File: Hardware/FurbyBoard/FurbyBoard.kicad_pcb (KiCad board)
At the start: 4 copper layers, 68.8 x 74.6 mm, 155 parts, among them J1 USB-C 16P, J11 J_EXP: header de expansión si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, J2 BAT+, J3 BAT-, J5 Micro I2S (3V3, GND, SCK, WS,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, J6 FPC 24P 0.5, J7 Frente: IR (emisor ×2, recept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, J8 Inclinación ×3, lengua ×2, al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, J9 Leva ×2, encoder ×4, barriga 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, Q1 SI7615ADN, Q2 AO3400A, Q3 AO3400A, SW1 RESET, SW2 BOOT, U1 USBLC6-2SC6, U10 TCA9535PWR, U11 SN74LVC1G17DBVR, U2 BQ24073RGTR, U3 TPS63802DLAR, U4 ESP32-S3-WROOM-1-N16R8, U5 TPS61089RNRR, U6 DRV8231ADSGR, U7 MAX98357AETE+T, U8 ME6211C28M5G-N, U9 ME6211C12M5G-N

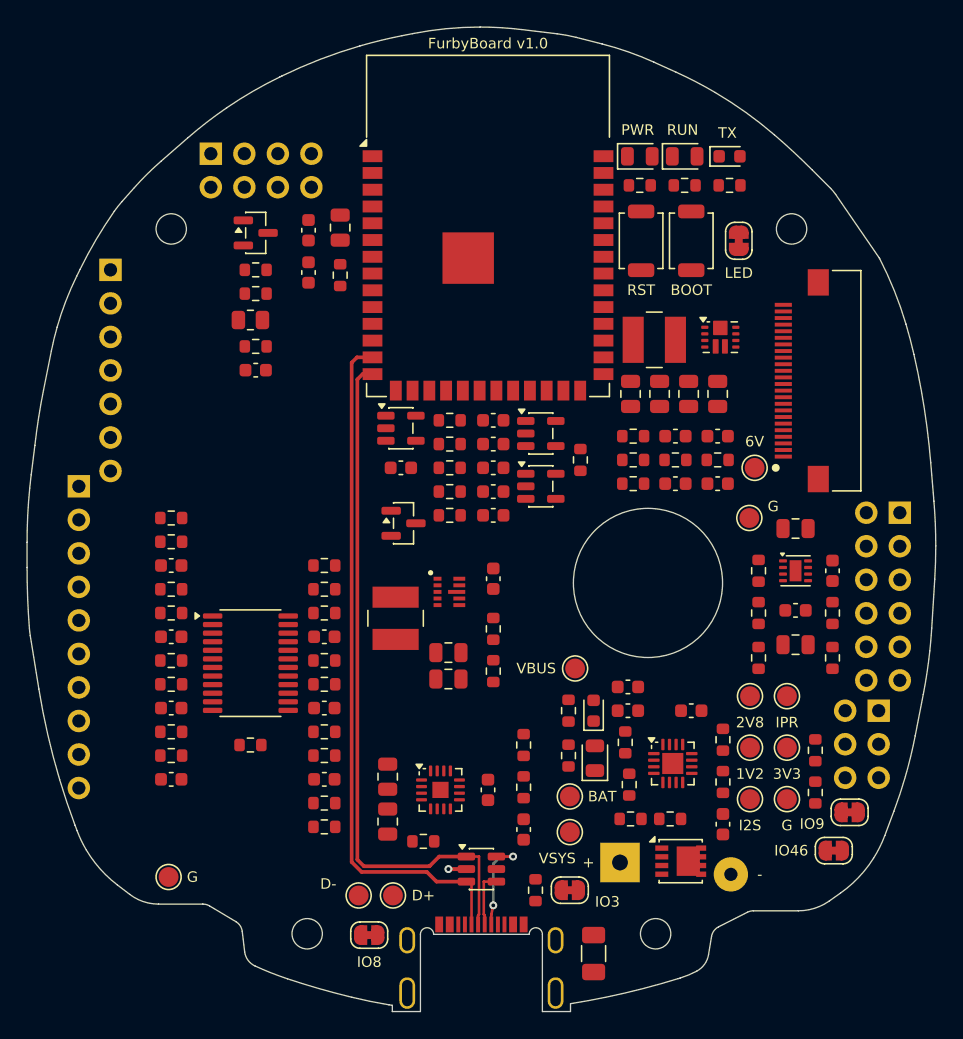
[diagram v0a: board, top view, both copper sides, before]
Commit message: Refactor: elevador de 6 V junto al DRV y al cargador, pasillo libre para la cámara
El bus DVP iba del módulo al FPC cruzando el bloque del TPS61089. El
elevador (U5, L2, C12-C19, R20-R24) pasa a la zona de abajo a la derecha,
entre el cargador (VSYS) y el puente H (V6), con el lazo de entrada y el de
salida cortos. El cargador se reordena con cada pasivo junto a su pin; los
LED de carga, junto al borde de la batería; JP1-JP3 al lóbulo izquierdo y al
del USB-C; R31/R32 junto a J5. comprobar_colocacion.py OK.

Co-Authored-By: Claude Opus 5.5 (1M context) <noreply@anthropic.com>
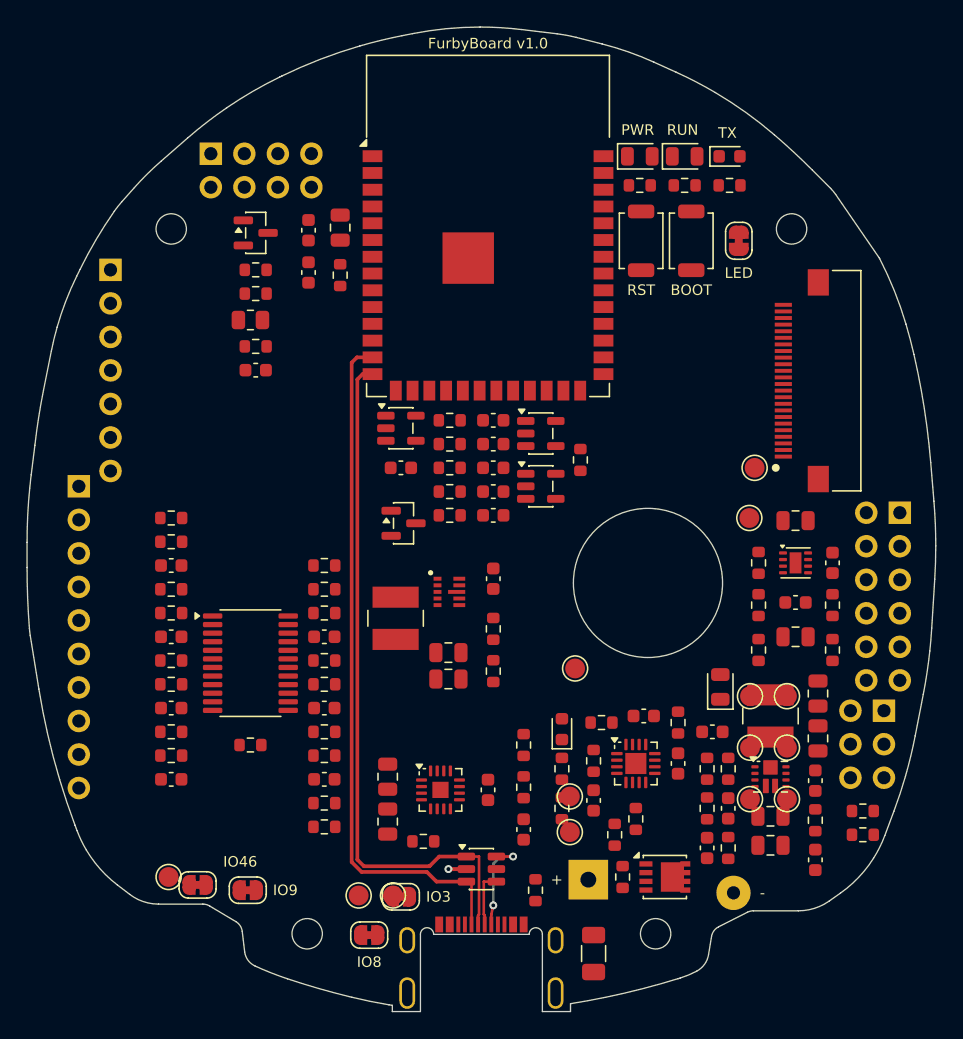
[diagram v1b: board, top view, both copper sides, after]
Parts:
- moved JP2 48.3 mm to (125.0, 78.2)
- moved JP1 46.0 mm to (128.8, 78.6)
- moved C19 34.4 mm to (168.4, 75.2), turned to 0 degrees
- moved U5 33.5 mm to (168.4, 70.0)
- moved C18 32.6 mm to (168.4, 73.0), turned to 0 degrees
- moved R21 30.3 mm to (165.2, 75.4), turned to 90 degrees
- moved L2 29.8 mm to (168.4, 65.4), turned to -90 degrees
- moved C15 29.4 mm to (171.8, 76.3), turned to 90 degrees
- moved C17 28.7 mm to (172.0, 67.1)
- moved C12 28.5 mm to (165.2, 72.4), turned to 90 degrees
- moved R23 28.3 mm to (171.8, 73.3), turned to 90 degrees
- moved C14 27.7 mm to (163.6, 75.4), turned to 90 degrees
- moved C13 27.1 mm to (171.8, 70.3), turned to 90 degrees
- moved C16 26.8 mm to (172.0, 63.7)
- moved R20 26.2 mm to (165.2, 69.4), turned to 90 degrees
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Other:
- board text removed: "1V2"
- board text removed: "2V8"
- board text removed: "6V"
- board text removed: "BAT"
- board text removed: "D+"
- board text removed: "D-"
- board text removed: "I2S"
- board text removed: "IPR"
- board text removed: "VBUS"

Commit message: Refactor: colocación final antes de rutar, con los TP junto a su fuente
- Amplificador (U7) junto a los pines del I2S del módulo y a los pads del
  altavoz (J8); deja libre la zona de abajo a la izquierda.
- Columnas de pasivos del expansor separadas de U10 para dejar pasillo de
  vías de GND.
- TP colocados y fijados antes de rutar: pad de 1,5 mm en la cara inferior
  sobre una vía de su red, junto al pin de su fuente; TP9 en el pin de
  I2S_DOUT del módulo. Lejos del logo y de los tornillos.
- aplicar.py: --fijar bloquea lo aplicado; rellenos exteriores solo con
  --rellenos.
- render/colocacion-arriba.png y colocacion-abajo.png.

DRC 0 infracciones, paridad OK; sin rutar.

Co-Authored-By: Claude Opus 5.5 (1M context) <noreply@anthropic.com>
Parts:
- TP1, TP10, TP11, TP12, TP13, TP14, TP2, TP3, TP4, TP5, TP6, TP7, TP8, TP9: moved to B.Cu
- moved TP9 50.6 mm to (137.0, 30.8), turned to 180 degrees
- moved C26 33.4 mm to (126.6, 44.5)
- moved U7 29.7 mm to (130.0, 44.5)
- moved C25 27.3 mm to (133.4, 46.8)
- moved C24 27.3 mm to (133.4, 43.4)
- moved TP6 27.0 mm to (144.7, 57.6), turned to 180 degrees
- moved TP7 25.2 mm to (168.7, 71.7), turned to 180 degrees
- moved TP10 25.1 mm to (151.9, 43.8), turned to 180 degrees
- moved TP11 25.0 mm to (151.9, 47.8), turned to 180 degrees
- moved TP1 21.3 mm to (155.7, 83.0), turned to 180 degrees
- moved TP13 20.6 mm to (166.0, 71.0), turned to 180 degrees
- moved TP12 20.4 mm to (143.0, 80.2), turned to 180 degrees
- moved TP14 19.4 mm to (170.9, 52.4), turned to 180 degrees
- moved TP8 12.0 mm to (168.0, 52.0), turned to 180 degrees
- moved TP5 8.86 mm to (160.5, 69.2), turned to 180 degrees
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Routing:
- net GND: track 1.36 -> 5.17 mm, vias 1 -> 4
- net IPROPI: track 0.00 -> 1.49 mm, vias 0 -> 1
- net I2S_DOUT: track 0.00 -> 0.89 mm, vias 0 -> 1
- net V6: track 0.00 -> 0.50 mm, vias 0 -> 1
- net VSYS: track 0.00 -> 0.45 mm, vias 0 -> 1
- net USB_DP: track 60.2 -> 60.7 mm, vias 2 -> 3
- net VBUS: track 0.00 -> 0.45 mm, vias 0 -> 1
- net CAM_DVDD: track 0.00 -> 0.45 mm, vias 0 -> 1
- net CAM_2V8: track 0.00 -> 0.45 mm, vias 0 -> 1
- net BAT: track 0.00 -> 0.45 mm, vias 0 -> 1
- net USB_DN: track 56.4 -> 56.8 mm, vias 0 -> 1
- net 3V3: track 0.00 -> 0.45 mm, vias 0 -> 1
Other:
- board text added: "1V2"
- board text added: "2V8"
- board text added: "6V"
- board text added: "BAT"
- board text added: "D+"
- board text added: "D-"
- board text added: "I2S"
- board text added: "VBUS"

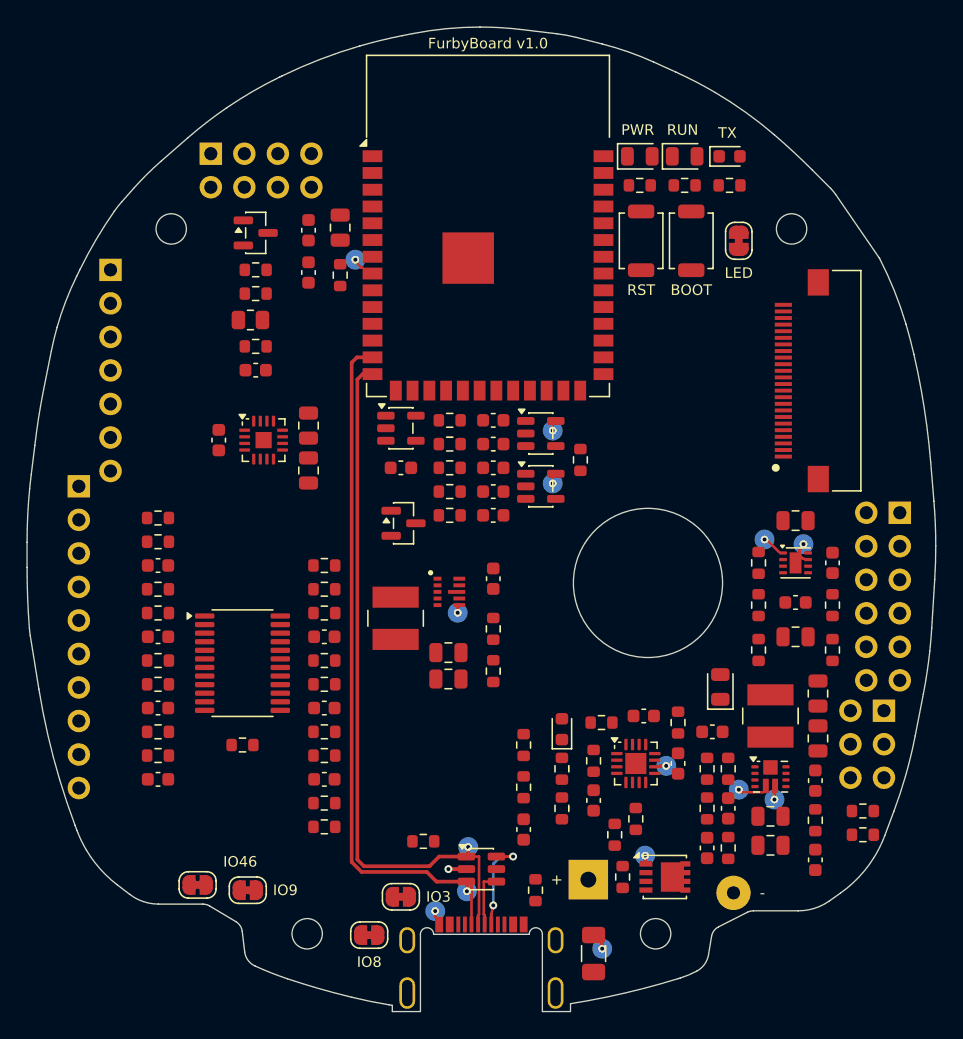
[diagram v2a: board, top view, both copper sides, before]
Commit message: Feature: lo crítico pre-rutado y fijado antes del autorrutado
- preparar.sh: colocación, TP, vías térmicas, pre-rutado y DSN en un paso.
- Pre-rutado con el rutador por rejilla (con su post-proceso) y fijado:
  lazos del TPS61089, del TPS63802 y del puente H, carga, batería, VSYS,
  V6, motor, altavoz, LED IR, 3V3 y bajadas de GND al plano (prerrutado.json,
  con 0,8 mm en los nodos de conmutación y 0,5-0,6 en potencia). C18/C19 giradas
  para que VOUT y GND del TPS61089 caigan sobre su condensador; compensación
  junto a su pin.
- vias_termicas.py: vías bajo los pads expuestos de U2, U7, U6 y U4.
- Amplificador fuera de la zona del logo (no admite vías).
- El DSN sale sin el relleno de VSYS de In2 (si no, tapa la capa).

DRC 0 infracciones, paridad OK; quedan 144 pads por unir.

Co-Authored-By: Claude Opus 5.5 (1M context) <noreply@anthropic.com>
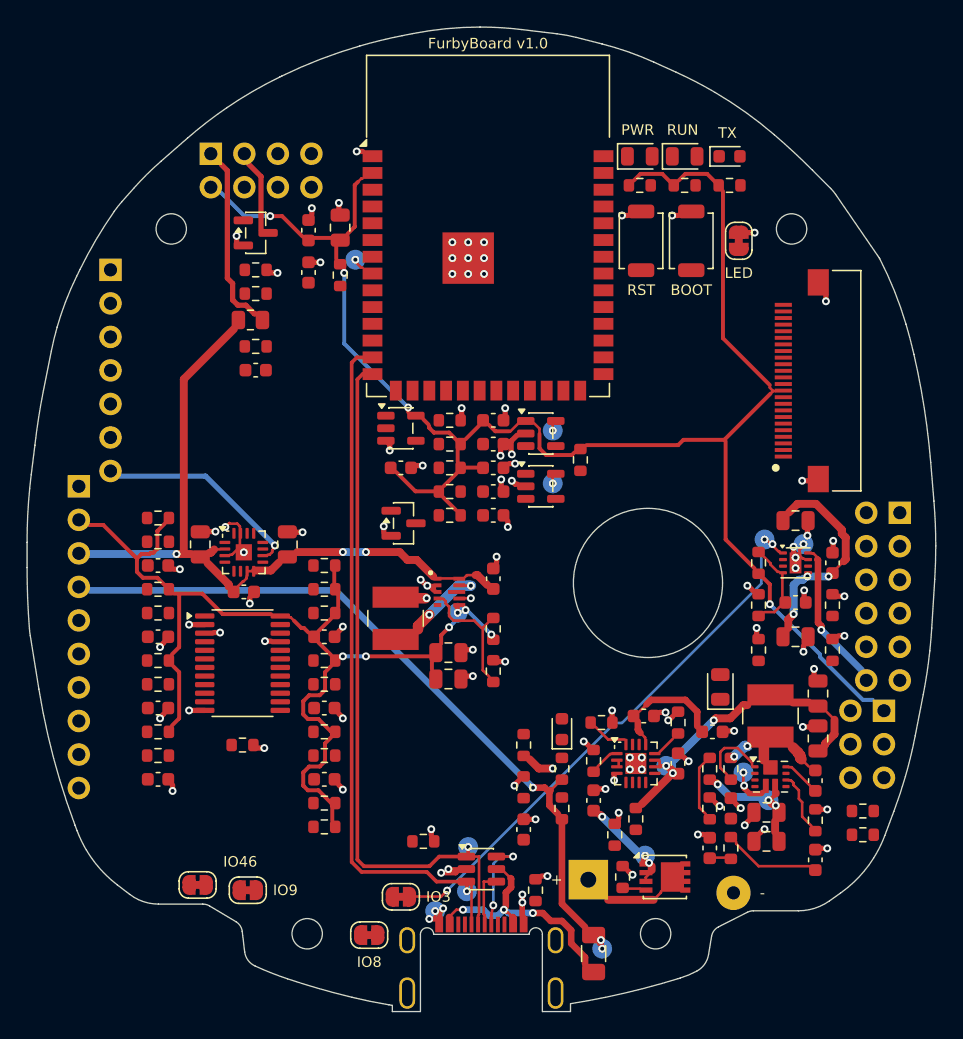
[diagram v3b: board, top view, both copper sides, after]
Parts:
- moved C26 11.7 mm to (128.5, 56.0), turned to 0 degrees
- moved C25 9.93 mm to (125.2, 52.4)
- moved C24 9.14 mm to (131.8, 52.4)
- moved U7 8.63 mm to (128.5, 53.0)
- moved C14 8.25 mm to (171.8, 76.3)
- moved C15 8.05 mm to (163.8, 75.4)
- moved R21 6.16 mm to (163.8, 69.4)
- moved R24 3.50 mm to (165.4, 75.4)
- moved R22 3.01 mm to (163.8, 72.4)
- moved TP13 1.35 mm to (166.4, 69.7)
- moved TP7 0.45 mm to (168.3, 71.8)
- moved C18 0.42 mm to (168.1, 72.7), turned to 180 degrees
- moved C19 0.42 mm to (168.1, 74.9), turned to 180 degrees
- moved C12 0.20 mm to (165.4, 72.4)
- moved R20 0.20 mm to (165.4, 69.4)
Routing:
- net 3V3: track 0.45 -> 178.4 mm, vias 1 -> 10
- net VSYS: track 0.45 -> 63.2 mm, vias 1 -> 6
- net VBUS: track 0.45 -> 60.8 mm, vias 1 -> 3
- net GND: track 5.17 -> 57.0 mm, vias 4 -> 102
- net IPROPI: track 1.49 -> 40.7 mm, vias 1 -> 3
- net V6: track 0.50 -> 20.1 mm, vias 1 -> 6
- net VBUS_IN: track 0.00 -> 16.8 mm, vias 0 -> 3
- net SPK_N: track 0.00 -> 14.9 mm, vias 0 -> 1
- net IR_LED_A: track 0.00 -> 12.8 mm
- net BAT: track 0.45 -> 12.6 mm, vias 1 -> 4
- net MOT_OUT2: track 0.00 -> 10.5 mm, vias 0 -> 1
- net BB_FB: track 0.00 -> 8.93 mm
- net BST_RC: track 0.00 -> 6.40 mm
- net BB_L1: track 0.00 -> 5.96 mm, vias 0 -> 2
- net IR_LED_K: track 0.00 -> 5.34 mm
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
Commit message: Feature: rutado de Freerouting importado y limpiado, con 25 conexiones pendientes
Una sola ejecución de Freerouting 1.9.0 (-mp 20, 10,5 min, sin red) sobre el
DSN con lo crítico fijado. limpiar.py une los tramos colineales, quita
repetidos y puntas colgando e informa de ángulos fuera de 0/45/90 (1, del
par USB fijo) y agudos (10).

Estado: 30 pads sin unir (≈ 25 conexiones), 7 pistas de In2 a menos de 0,3
del borde (la franja del DSN solo cubría F y B) y 23 puntas colgando por
revisar. render/rutado-pendiente.png marca lo que falta.

Co-Authored-By: Claude Opus 5.5 (1M context) <noreply@anthropic.com>
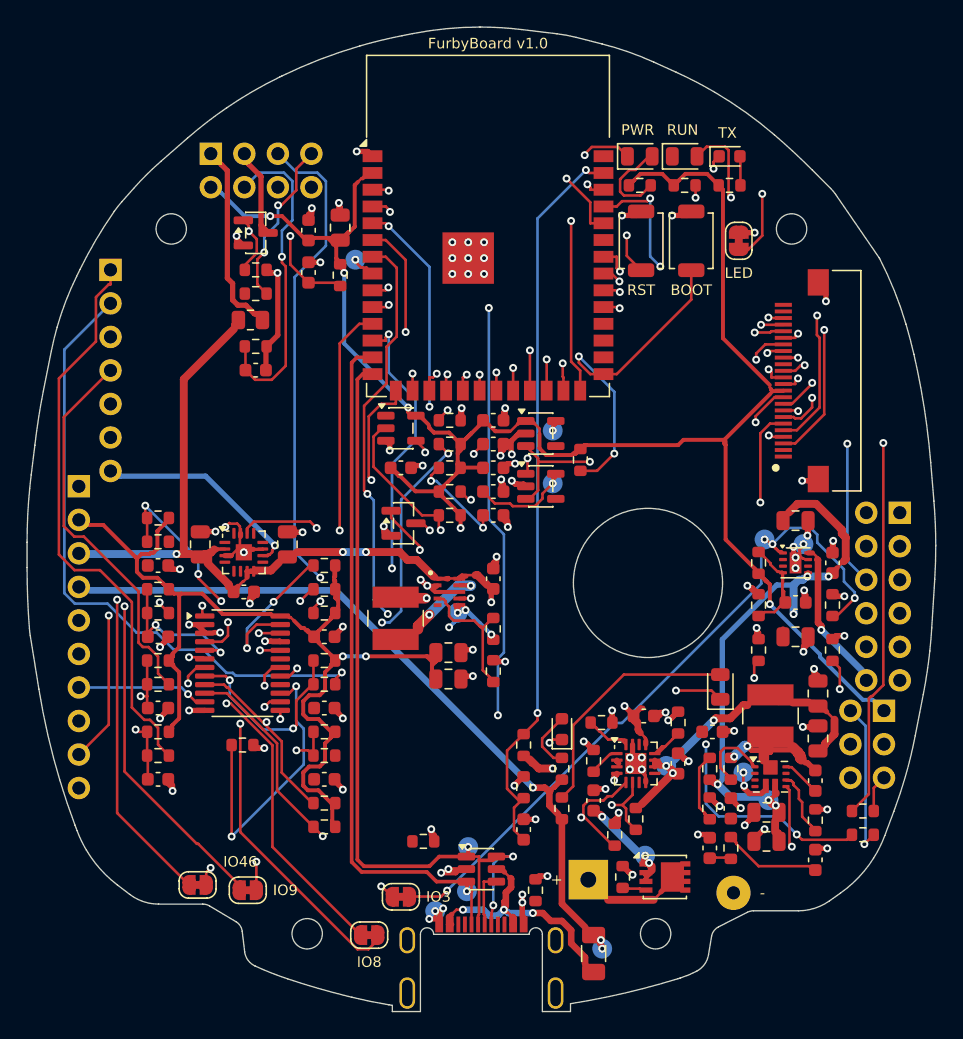
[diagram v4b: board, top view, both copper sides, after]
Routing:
- net I2C_SDA: track 0.00 -> 120.0 mm, vias 0 -> 4
- net I2C_SCL: track 0.00 -> 111.0 mm, vias 0 -> 5
- net EN_6V: track 0.00 -> 94.2 mm, vias 0 -> 4
- net I2S_WS: track 0.00 -> 86.3 mm, vias 0 -> 5
- net U0RX: track 0.00 -> 83.5 mm, vias 0 -> 1
- net U0TX: track 0.00 -> 81.3 mm, vias 0 -> 4
- net I2S_BCLK: track 0.00 -> 77.3 mm, vias 0 -> 2
- net I2S_DIN: track 0.00 -> 73.8 mm, vias 0 -> 1
- net BACK_PAD: track 0.00 -> 71.9 mm, vias 0 -> 2
- net GND: track 57.0 -> 118.8 mm
- net ENC_IO: track 0.00 -> 60.6 mm, vias 0 -> 3
- net HOME: track 0.00 -> 60.1 mm, vias 0 -> 4
- net IPROPI_IO: track 0.00 -> 59.7 mm, vias 0 -> 2
- net PGOOD: track 0.00 -> 59.4 mm, vias 0 -> 2
- net CAM_PWDN: track 0.00 -> 59.1 mm, vias 0 -> 4
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
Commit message: Feature: remate R5 del rutado, de 30 a 15 pads sin unir
Cuello de DP en J1 a 45° + vertical sin mover la vía. Sin pistas de In2
junto al borde, sin puntas ni ángulos agudos. Cobre de U5, U2, U7 y U6
rehecho por rejilla; TP13 movido con su vía. DRC con paridad: 15 pads sin
unir y 2 vías de IR_RX a medio camino. Mapa en render/.

Co-Authored-By: Claude Opus 5.5 (1M context) <noreply@anthropic.com>
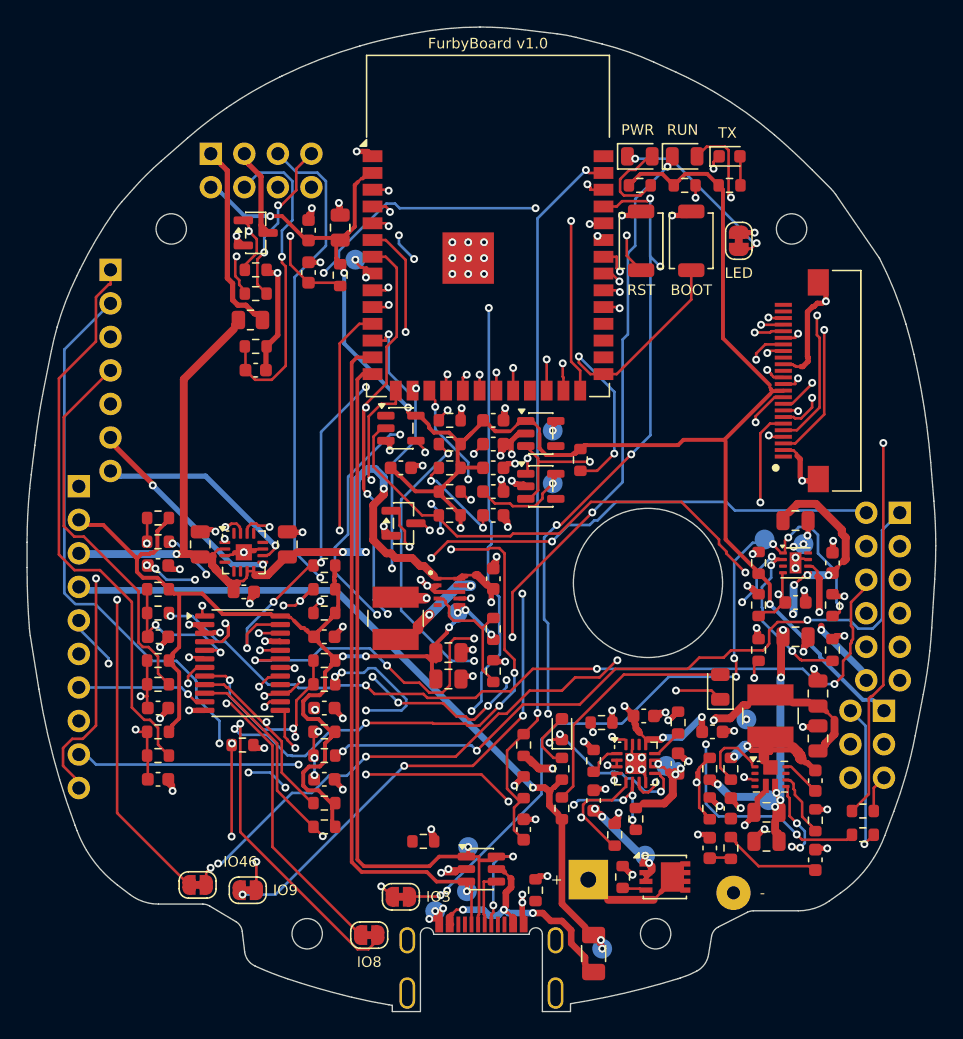
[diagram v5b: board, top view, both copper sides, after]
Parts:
- moved TP13 4.03 mm to (166.6, 65.7)
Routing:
- net TUMMY_PAD: track 0.00 -> 81.0 mm, vias 0 -> 6
- net LED_RUN_K: track 0.00 -> 66.9 mm, vias 0 -> 6
- net HOME_PAD: track 0.00 -> 55.1 mm, vias 0 -> 3
- net ENC_IO: track 60.6 -> 90.3 mm, vias 3 -> 8
- net CAM_Y7: track 25.1 -> 0.00 mm, vias 2 -> 0
- net I2S_DOUT: track 1.82 -> 26.3 mm, vias 1 -> 3
- net CAM_Y8: track 26.1 -> 2.02 mm, vias 2 -> 1
- net TILT_B_PAD: track 48.2 -> 71.8 mm, vias 1 -> 6
- net CAM_PWDN: track 59.1 -> 76.8 mm, vias 4 -> 8
- net I2C_SCL: track 111.0 -> 126.5 mm, vias 5 -> 7
- net SPK_P: track 0.00 -> 15.1 mm, vias 0 -> 2
- net I2C_SDA: track 120.0 -> 107.1 mm, vias 4 -> 7
- net U0RX: track 83.5 -> 71.9 mm, vias 1 -> 4
- net CHG: track 36.7 -> 47.7 mm, vias 2 -> 4
- net U0TX: track 81.3 -> 92.2 mm, vias 4 -> 7
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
